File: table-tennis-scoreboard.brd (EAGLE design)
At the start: 68.6 x 53.3 mm, 8 parts

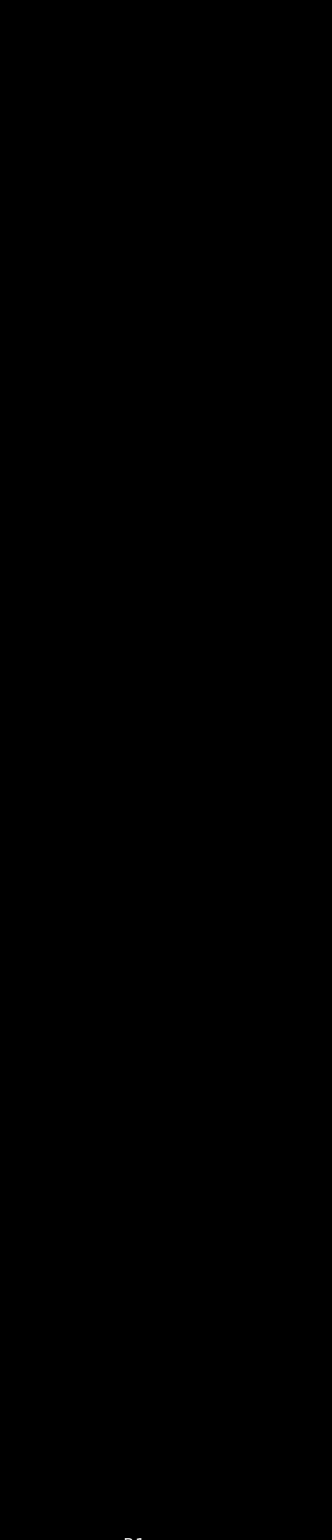
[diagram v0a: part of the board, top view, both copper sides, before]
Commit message: add buttons and second display group
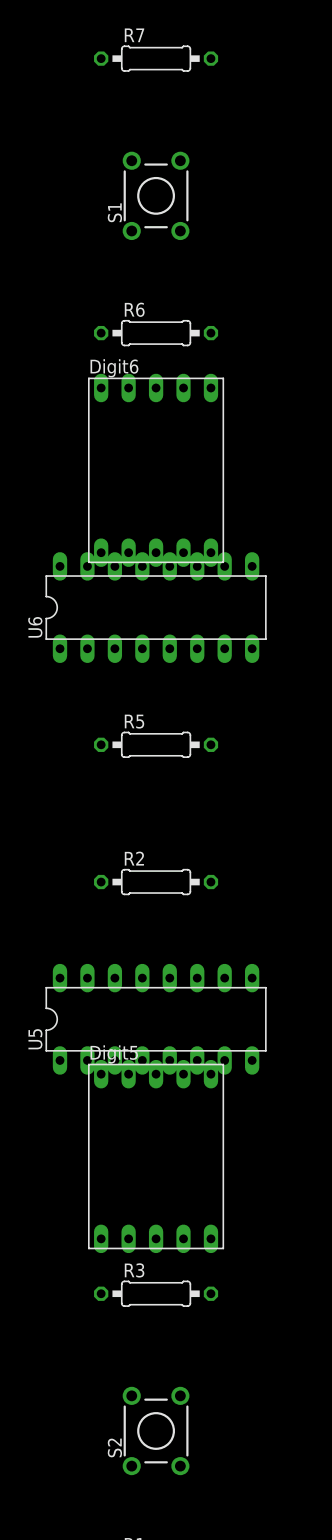
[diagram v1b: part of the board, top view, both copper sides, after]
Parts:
- added Digit5, Digit6: (no value), AUTODESK_CIRCUITS_BREADBOARD:HDSP-M
- added R2, R3, R5, R6, R7: 1k‎Ω, AUTODESK_CIRCUITS_BREADBOARD:0207/10
- added S1, S2: (no value), AUTODESK_CIRCUITS_BREADBOARD:TL1105
- added U5, U6: (no value), AUTODESK_CIRCUITS_BREADBOARD:DIL16
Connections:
- removed net N$15 (its old number): R1.2, R10.2, R4.2, U2.GND..
- removed net N$9 (its old number): U1.13
- new net N$22: R3.2, S2.3
- new net N$24: S2.4, U1.10, U1.16, U2.5V, U3.10, U3.16, U5.10, U5.16, U6.10, U6.16
- new net N$25: R1.2, R10.2, R2.2, R3.1, R4.2, R5.2, R6.2, R7.1, S1.4, U1.13, U2.GND.., U3.13, U5.13, U6.13
- new net N$26: U2.10, U5.11, U6.11
- new net N$27: Digit5.10, U5.6
- new net N$29: Digit5.9, U5.5
- new net N$30: Digit5.1, U5.4
- new net N$31: Digit5.2, U5.3
- new net N$32: Digit5.7, U5.15
- new net N$33: Digit5.4, U5.2
- new net N$34: Digit5.6, U5.1
- new net N$35: Digit6.7, U6.15
- new net N$36: Digit6.6, U6.1
- new net N$37: Digit6.4, U6.2
- new net N$38: Digit6.2, U6.3
- new net N$39: Digit6.1, U6.4
- new net N$40: Digit6.9, U6.5
- new net N$41: Digit6.10, U6.6
- new net N$42: U5.9, U6.14
- new net N$43: U2.8, U5.14
- new net N$44: S1.1, U2.3
- new net N$45: R7.2, S1.3
- new net N$46: Digit5.8, Digit6.8, R5.1
- new net N$47: R6.1, U6.8
- new net N$48: U6.9
- new net N$49: U6.7
- new net N$50: R2.1, U5.8
- new net N$51: U5.7
- net N$23: now also S2.1, U2.2; no longer U3.13
- net N$28: now also U2.9, U5.12, U6.12; no longer U1.10, U1.16, U2.5V, U3.10, U3.16

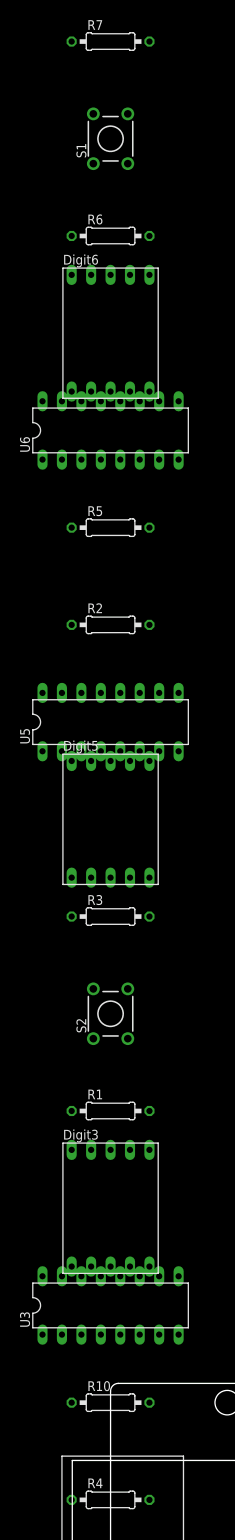
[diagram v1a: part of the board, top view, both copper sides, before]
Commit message: fix error with inverted display
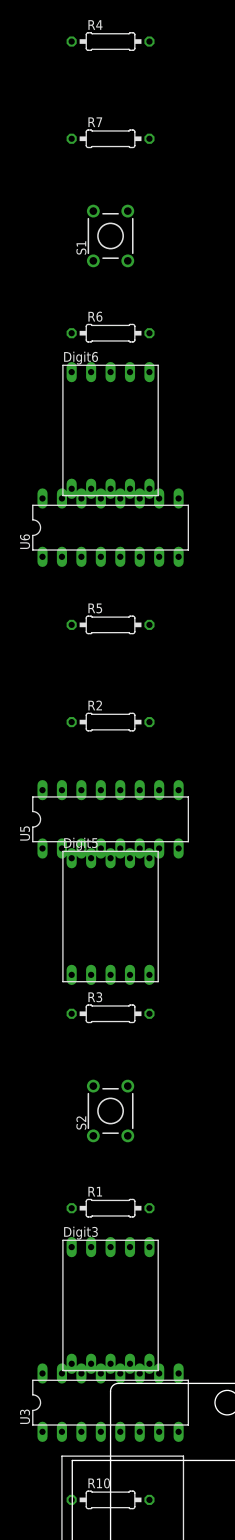
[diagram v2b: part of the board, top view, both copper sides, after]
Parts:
- moved R4 190.5 mm to (5.00, 238.7)
- moved Digit6 12.7 mm to (5.00, 187.9)
- moved R2 12.7 mm to (5.00, 149.8)
- moved R5 12.7 mm to (5.00, 162.5)
- moved R6 12.7 mm to (5.00, 200.6)
- moved R7 12.7 mm to (5.00, 226.0)
- moved S1 12.7 mm to (5.00, 213.3)
- moved U5 12.7 mm to (5.00, 137.1)
- moved U6 12.7 mm to (5.00, 175.2)
- moved Digit3 12.7 mm to (5.00, 73.6)
- moved Digit5 12.7 mm to (5.00, 124.4)
- moved R1 12.7 mm to (5.00, 86.3)
- moved R3 12.7 mm to (5.00, 111.7)
- moved S2 12.7 mm to (5.00, 99.0)
- moved U3 12.7 mm to (5.00, 60.9)
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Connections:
- removed net N$24 (its old number): S2.4, U1.10, U1.16, U2.5V, U3.10, U3.16, U5.10, U5.16, U6.10, U6.16
- removed net N$25 (its old number): R1.2, R10.2, R2.2, R3.1, R4.2, R5.2, R6.2, R7.1, S1.4, U1.13, U2.GND.., U3.13, U5.13, U6.13
- new net N$23: R1.2, R10.2, R2.2, R3.2, R4.2, R5.2, R6.2, R7.1, U1.13, U2.GND.., U3.13, U5.13, U6.13
- new net N$51: R3.1, S2.3
- net N$15: now also Digit3.5
- net N$22: now also S1.4, S2.4, U1.10, U1.16, U2.5V, U3.10, U3.16, U5.10, U5.16, U6.10, U6.16; no longer R3.2, S2.3
- net N$3: now also Digit1.5

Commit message: add set points counters
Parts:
- removed R2, R5, R6: 1k‎Ω, AUTODESK_CIRCUITS_BREADBOARD:0207/10
- added Digit2, Digit4: (no value), AUTODESK_CIRCUITS_BREADBOARD:HDSP-M
- added R9: 1k‎Ω, AUTODESK_CIRCUITS_BREADBOARD:0207/10
- added U4, U7: (no value), AUTODESK_CIRCUITS_BREADBOARD:DIL16
- moved R3 165.1 mm to (5.00, 276.8)
- moved R4 63.5 mm to (5.00, 175.2)
- moved S1 50.8 mm to (5.00, 162.5)
- moved Digit6 38.1 mm to (5.00, 149.8)
- moved U6 38.1 mm to (5.00, 137.1)
- moved R7 25.4 mm to (5.00, 251.4)
- moved Digit5 12.7 mm to (5.00, 111.7)
- moved U5 12.7 mm to (5.00, 124.4)
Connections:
- removed net N$22 (its old number): S1.4, S2.4, U1.10, U1.16, U2.5V, U3.10, U3.16, U5.10, U5.16, U6.10, U6.16
- removed net N$24 (its old number): U2.10, U5.11, U6.11
- removed net N$26 (its old number): U2.9, U5.12, U6.12
- removed net N$44 (its old number): U6.9
- removed net N$46 (its old number): R2.1, U5.8
- removed net N$48 (its old number): U1.11, U2.7, U3.11
- removed net N$49 (its old number): U1.12, U2.6, U3.12
- new net N$20: U3.9, U7.14
- new net N$39: U4.14, U6.9
- new net N$50: Digit2.6, U4.1
- new net N$51: Digit2.1, U4.4
- new net N$52: Digit2.10, U4.6
- new net N$53: U4.7
- new net N$54: Digit2.4, U4.2
- new net N$55: Digit2.9, U4.5
- new net N$56: Digit2.2, U4.3
- new net N$57: U4.9
- new net N$58: Digit2.7, U4.15
- new net N$59: Digit4.6, U7.1
- new net N$60: Digit4.1, U7.4
- new net N$61: Digit4.10, U7.6
- new net N$62: Digit4.2, U7.7
- new net N$63: U7.8
- new net N$64: Digit4.4, U7.2
- new net N$65: R1.2, R10.2, R3.1, R3.2, R4.2, R7.1, R9.2, U1.13, U2.GND.., U3.13, U7.13
- new net N$66: Digit4.9, U7.5
- new net N$67: Digit4.7, U7.15
- new net N$68: Digit4.5, U7.3
- new net N$69: U7.9
- new net N$70: S1.4, S2.4, U1.10, U1.16, U2.5V, U3.10, U3.16, U4.10, U4.16, U5.10, U5.16, U6.10, U6.16, U7.10, U7.16
- new net N$71: Digit2.8, Digit5.8, Digit6.8, R9.1, U4.13, U4.8, U5.13, U5.8, U6.13, U6.8
- new net N$72: Digit4.8, R3.2
- net N$21: now also U2.10, U4.11, U5.11, U6.11; no longer U3.9
- net N$23: now also U2.9, U4.12, U5.12, U6.12; no longer R1.2, R10.2, R2.2, R3.2, R4.2, R5.2, R6.2, R7.1, U1.13, U2.GND.., U3.13, U5.13, U6.13
- net N$42: now also U1.11, U2.7, U3.11, U7.11; no longer Digit5.8, Digit6.8, R5.1
- net N$43: now also U1.12, U2.6, U3.12, U7.12; no longer R6.1, U6.8
